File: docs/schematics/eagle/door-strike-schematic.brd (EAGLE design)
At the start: 100 x 80 mm, 9 parts, among them T1 TIP120

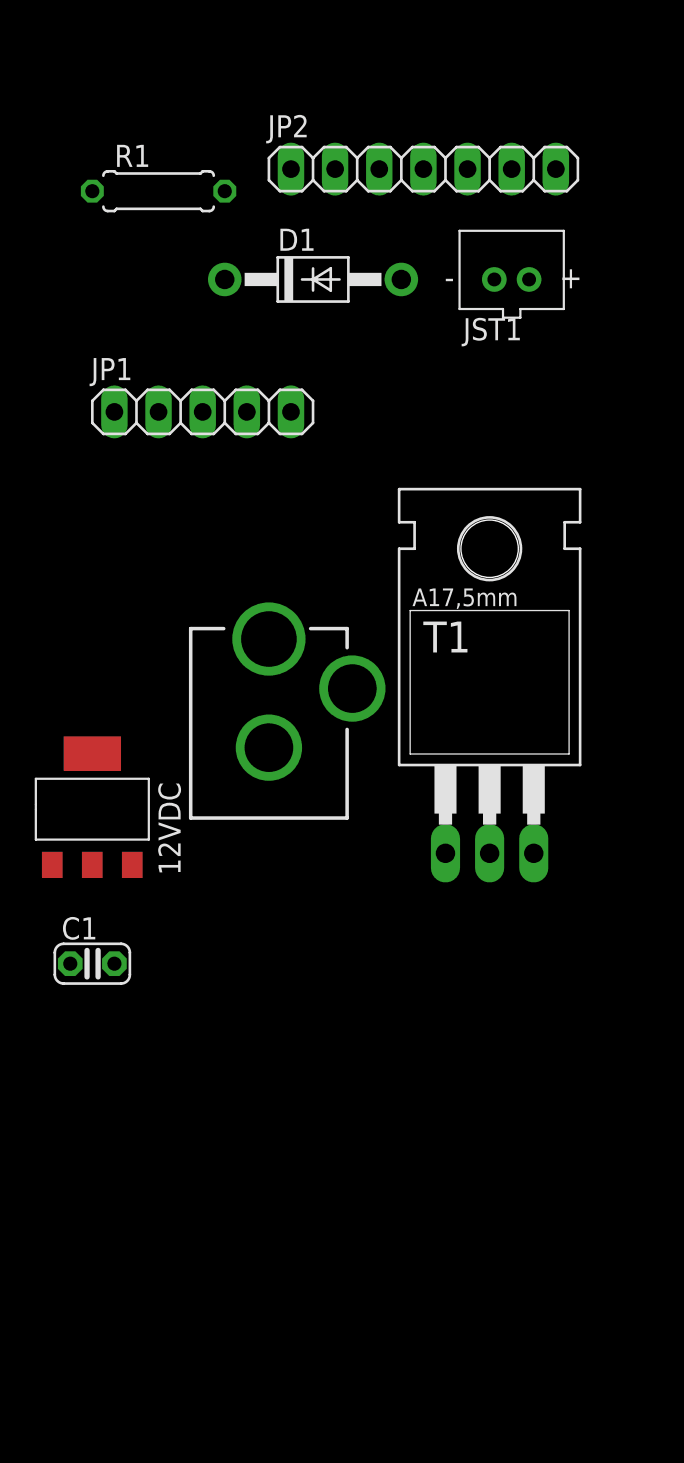
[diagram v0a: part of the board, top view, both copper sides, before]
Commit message: updated schema with RFduino component and caps for voltage regulation
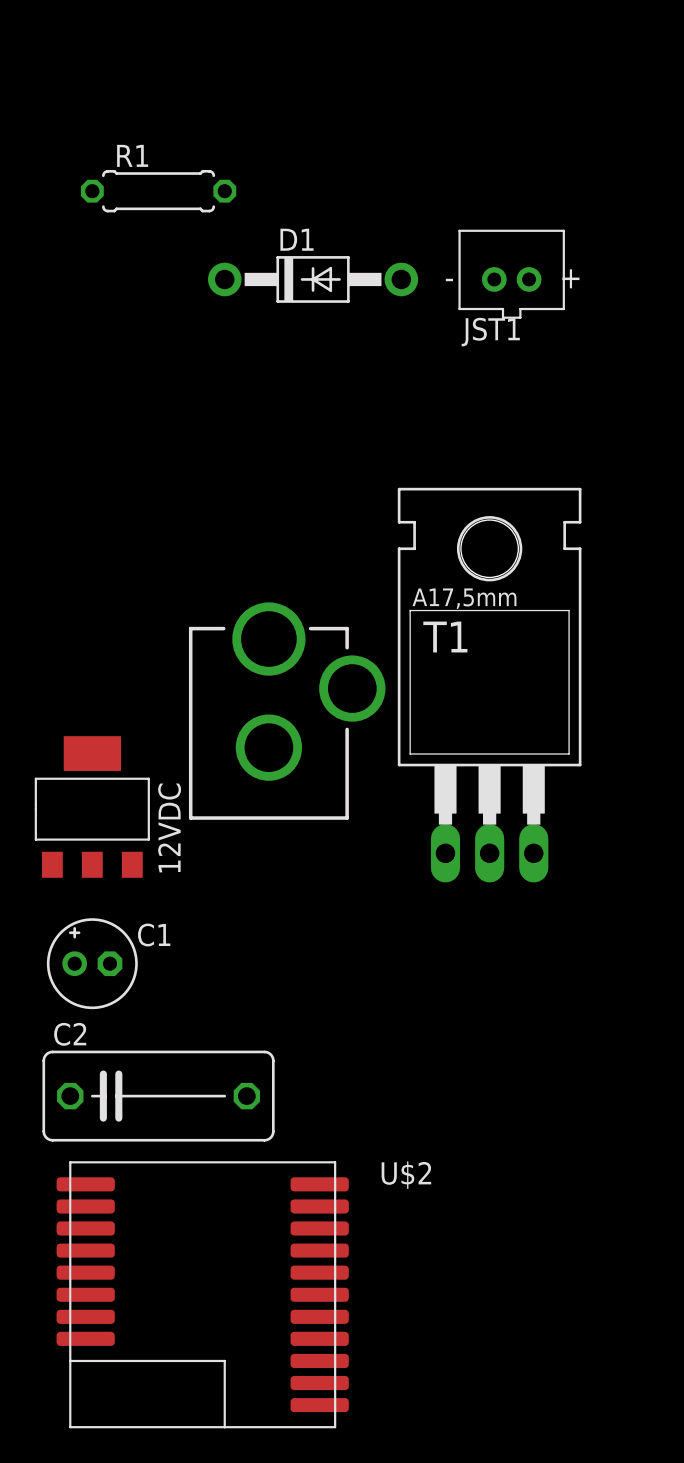
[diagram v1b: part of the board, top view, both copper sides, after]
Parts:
- removed JP1: NO FUNCTION, STABILITY ONLY, pinhead:1X05
- removed JP2: (no value), pinhead:1X07
- added C2: .1uF, adafruit:C102-054X133
- added U$2: RFD22301, RFD22301-11.25.13:RFD21733
- C1: value .0047uF -> 10uF; device adafruit:C025-024X044 -> adafruit:E2-5
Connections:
- removed net N$5: JP2.5
- removed net N$6 (its old number): C1.1, D1.C
- net GND: now also C1.-, C2.2; no longer JP2.1
- net N$1: now also R1.1, U$2.P$6; no longer R1.2, T1.B
- net N$2: now also R1.2; no longer R1.1
- net N$7: now also C1.+, U$2.P$13
- net N$8: now also C2.1, D1.C, U$1.VIN; no longer C1.2
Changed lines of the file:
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@@
 <element name="12VDC" library="adafruit" package="DCJACK_2MM_PTH" value="" x="-31.75" y="1.27"/>
 <element name="D1" library="adafruit" package="DO41-10" value="1N4004" x="-29.21" y="35.56"/>
-<element name="JP1" library="pinhead" package="1X05" value="NO FUNCTION, STABILITY ONLY" x="-35.56" y="27.94"/>
-<element name="JP2" library="pinhead" package="1X07" value="" x="-22.86" y="41.91"/>
 <element name="JST1" library="adafruit" package="JST-PH-2-THM" value="SOL" x="-17.78" y="35.56"/>
 <element name="R1" library="resistor" package="0207/7" value="2.2K" x="-38.1" y="40.64"/>
 <element name="T1" library="transistor-power" package="TO220AH" value="TIP120" x="-19.05" y="8.89"/>
 <element name="U$1" library="LD1117" package="LD1117SOT-223" value="LD1117" x="-41.91" y="5.08"/>
-<element name="C1" library="adafruit" package="C025-024X044" value=".0047uF" x="-41.91" y="-3.81"/>
+<element name="C1" library="adafruit" package="E2-5" value="10uF" x="-41.91" y="-3.81"/>
+<element name="C2" library="adafruit" package="C102-054X133" value=".1uF" x="-38.1" y="-11.43"/>
+<element name="U$2" library="RFD22301-11.25.13" package="RFD21733" value="RFD22301" x="-35.56" y="-22.86"/>
 </elements>
 <signals>
@@
 <contactref element="12VDC" pad="GNDBREAK"/>
 </signal>
-<signal name="N$1">
-<contactref element="R1" pad="2"/>
-<contactref element="T1" pad="B"/>
-<wire x1="-34.29" y1="40.64" x2="-21.59" y2="2.54" width="0" layer="19" extent="1-1"/>
-</signal>
 <signal name="GND">
 <contactref element="T1" pad="E"/>
-<contactref element="JP2" pad="1"/>
 <contactref element="U$1" pad="GND"/>
 <contactref element="12VDC" pad="GND"/>
+<contactref element="C2" pad="2"/>
+<contactref element="C1" pad="-"/>
+<wire x1="-40.894" y1="-3.81" x2="-44.21" y2="1.88" width="0" layer="19" extent="1-1"/>
+<wire x1="-33.02" y1="-11.43" x2="-40.894" y2="-3.81" width="0" layer="19" extent="1-1"/>
 <wire x1="-31.75" y1="8.62" x2="-44.21" y2="1.88" width="0" layer="19" extent="1-1"/>
 <wire x1="-16.51" y1="2.54" x2="-31.75" y2="8.62" width="0" layer="19" extent="1-1"/>
-<wire x1="-30.48" y1="41.91" x2="-31.75" y2="8.62" width="0" layer="19" extent="1-1"/>
 </signal>
-<signal name="N$3">
+<signal name="N$8">
+<contactref element="12VDC" pad="PWR"/>
+<contactref element="U$1" pad="VIN"/>
+<contactref element="C2" pad="1"/>
+<contactref element="D1" pad="C"/>
+<wire x1="-39.61" y1="1.88" x2="-43.18" y2="-11.43" width="0" layer="19" extent="1-1"/>
+<wire x1="-31.75" y1="14.87" x2="-39.61" y2="1.88" width="0" layer="19" extent="1-1"/>
+<wire x1="-34.29" y1="35.56" x2="-31.75" y2="14.87" width="0" layer="19" extent="1-1"/>
+</signal>
+<signal name="N$7">
+<contactref element="U$1" pad="(VOUT)"/>
+<contactref element="U$1" pad="VOUT"/>
+<contactref element="C1" pad="+"/>
+<contactref element="U$2" pad="P$13"/>
+<wire x1="-42.926" y1="-3.81" x2="-28.829" y2="-24.13" width="0" layer="19" extent="1-1"/>
+<wire x1="-41.91" y1="1.88" x2="-42.926" y2="-3.81" width="0" layer="19" extent="1-1"/>
+<wire x1="-41.91" y1="8.28" x2="-41.91" y2="1.88" width="0" layer="19" extent="1-1"/>
+</signal>
+<signal name="N$6">
 <contactref element="T1" pad="C"/>
 <contactref element="D1" pad="A"/>
 <wire x1="-24.13" y1="35.56" x2="-19.05" y2="2.54" width="0" layer="19" extent="1-1"/>
 </signal>
-<signal name="N$8">
-<contactref element="12VDC" pad="PWR"/>
-<contactref element="C1" pad="2"/>
-<wire x1="-31.75" y1="14.87" x2="-40.64" y2="-3.81" width="0" layer="19" extent="1-1"/>
+<signal name="N$1">
+<contactref element="R1" pad="1"/>
+<contactref element="U$2" pad="P$6"/>
+<wire x1="-41.91" y1="40.64" x2="-42.291" y2="-22.86" width="0" layer="19" extent="1-1"/>
 </signal>
 <signal name="N$2">
-<contactref element="R1" pad="1"/>
-</signal>
-<signal name="N$5">
-<contactref element="JP2" pad="5"/>
-</signal>
-<signal name="N$7">
-<contactref element="U$1" pad="(VOUT)"/>
-<contactref element="U$1" pad="VOUT"/>
-<wire x1="-41.91" y1="8.28" x2="-41.91" y2="1.88" width="0" layer="19" extent="1-1"/>
-</signal>
-<signal name="N$6">
-<contactref element="D1" pad="C"/>
-<contactref element="C1" pad="1"/>
-<wire x1="-34.29" y1="35.56" x2="-43.18" y2="-3.81" width="0" layer="19" extent="1-1"/>
+<contactref element="R1" pad="2"/>
 </signal>
 </signals>

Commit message: cleaned up board organization and added label for LD1117 IC
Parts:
- renumbered U$1 to IC1
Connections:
- net GND: now also U$2.P$8
- net N$8: no longer IC1.VIN
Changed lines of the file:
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@@
 <?xml version="1.0" encoding="utf-8"?>
 <!DOCTYPE eagle SYSTEM "eagle.dtd">
-<eagle version="7.2.0">
+<eagle version="7.3.0">
 <drawing>
 <settings>
@@
 <element name="R1" library="resistor" package="0207/7" value="2.2K" x="-38.1" y="40.64"/>
 <element name="T1" library="transistor-power" package="TO220AH" value="TIP120" x="-19.05" y="8.89"/>
-<element name="U$1" library="LD1117" package="LD1117SOT-223" value="LD1117" x="-41.91" y="5.08"/>
+<element name="IC1" library="LD1117" package="LD1117SOT-223" value="LD1117" x="-41.91" y="5.08"/>
 <element name="C1" library="adafruit" package="E2-5" value="10uF" x="-41.91" y="-3.81"/>
 <element name="C2" library="adafruit" package="C102-054X133" value=".1uF" x="-38.1" y="-11.43"/>
@@
 <signal name="GND">
 <contactref element="T1" pad="E"/>
-<contactref element="U$1" pad="GND"/>
+<contactref element="IC1" pad="GND"/>
 <contactref element="12VDC" pad="GND"/>
+<contactref element="C1" pad="-"/>
+<contactref element="U$2" pad="P$8"/>
 <contactref element="C2" pad="2"/>
-<contactref element="C1" pad="-"/>
-<wire x1="-40.894" y1="-3.81" x2="-44.21" y2="1.88" width="0" layer="19" extent="1-1"/>
-<wire x1="-33.02" y1="-11.43" x2="-40.894" y2="-3.81" width="0" layer="19" extent="1-1"/>
+<wire x1="-33.02" y1="-11.43" x2="-42.291" y2="-25.4" width="0" layer="19" extent="1-1"/>
+<wire x1="-40.894" y1="-3.81" x2="-33.02" y2="-11.43" width="0" layer="19" extent="1-1"/>
+<wire x1="-44.21" y1="1.88" x2="-40.894" y2="-3.81" width="0" layer="19" extent="1-1"/>
 <wire x1="-31.75" y1="8.62" x2="-44.21" y2="1.88" width="0" layer="19" extent="1-1"/>
 <wire x1="-16.51" y1="2.54" x2="-31.75" y2="8.62" width="0" layer="19" extent="1-1"/>
@@
 <signal name="N$8">
 <contactref element="12VDC" pad="PWR"/>
-<contactref element="U$1" pad="VIN"/>
+<contactref element="D1" pad="C"/>
 <contactref element="C2" pad="1"/>
-<contactref element="D1" pad="C"/>
-<wire x1="-39.61" y1="1.88" x2="-43.18" y2="-11.43" width="0" layer="19" extent="1-1"/>
-<wire x1="-31.75" y1="14.87" x2="-39.61" y2="1.88" width="0" layer="19" extent="1-1"/>
+<wire x1="-31.75" y1="14.87" x2="-43.18" y2="-11.43" width="0" layer="19" extent="1-1"/>
 <wire x1="-34.29" y1="35.56" x2="-31.75" y2="14.87" width="0" layer="19" extent="1-1"/>
 </signal>
 <signal name="N$7">
-<contactref element="U$1" pad="(VOUT)"/>
-<contactref element="U$1" pad="VOUT"/>
+<contactref element="U$2" pad="P$13"/>
+<contactref element="IC1" pad="(VOUT)"/>
+<contactref element="IC1" pad="VOUT"/>
 <contactref element="C1" pad="+"/>
-<contactref element="U$2" pad="P$13"/>
 <wire x1="-42.926" y1="-3.81" x2="-28.829" y2="-24.13" width="0" layer="19" extent="1-1"/>
 <wire x1="-41.91" y1="1.88" x2="-42.926" y2="-3.81" width="0" layer="19" extent="1-1"/>

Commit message: more schematic organization
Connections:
- new net N$3: U$2.P$8
- new net N$4: C2.2
- net GND: no longer C2.2, U$2.P$8
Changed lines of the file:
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@@
 <contactref element="12VDC" pad="GND"/>
 <contactref element="C1" pad="-"/>
-<contactref element="U$2" pad="P$8"/>
-<contactref element="C2" pad="2"/>
-<wire x1="-33.02" y1="-11.43" x2="-42.291" y2="-25.4" width="0" layer="19" extent="1-1"/>
-<wire x1="-40.894" y1="-3.81" x2="-33.02" y2="-11.43" width="0" layer="19" extent="1-1"/>
-<wire x1="-44.21" y1="1.88" x2="-40.894" y2="-3.81" width="0" layer="19" extent="1-1"/>
+<wire x1="-40.894" y1="-3.81" x2="-44.21" y2="1.88" width="0" layer="19" extent="1-1"/>
 <wire x1="-31.75" y1="8.62" x2="-44.21" y2="1.88" width="0" layer="19" extent="1-1"/>
 <wire x1="-16.51" y1="2.54" x2="-31.75" y2="8.62" width="0" layer="19" extent="1-1"/>
@@
 <contactref element="R1" pad="2"/>
 </signal>
+<signal name="N$4">
+<contactref element="C2" pad="2"/>
+</signal>
+<signal name="N$3">
+<contactref element="U$2" pad="P$8"/>
+</signal>
 </signals>
